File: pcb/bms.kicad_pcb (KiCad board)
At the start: 2 copper layers, 202 x 60 mm, 47 parts, among them J1 C0, J10 Taps 6-8, J11 Taps 0-5, J12 Taps 6-8, J13 Taps 0-5, J2 C1, J3 C2, J4 C3, J5 C4, J6 C5, J7 C6, J8 C7, J9 C8, U1 BQ76942PFBR

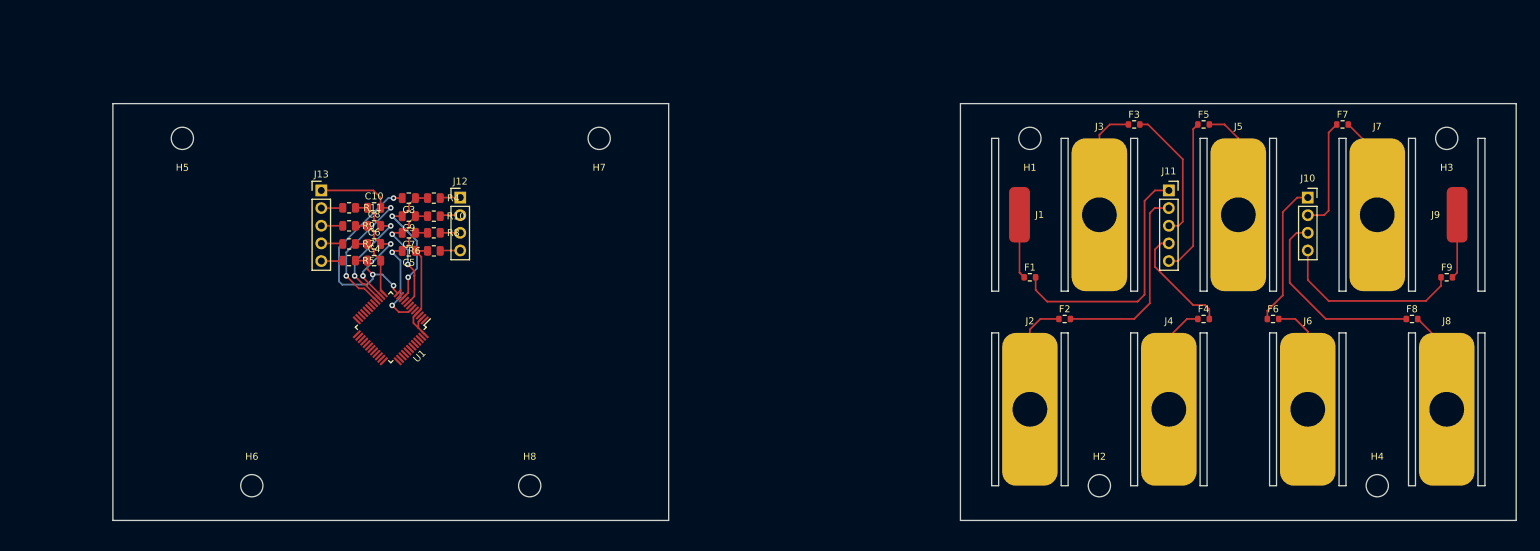
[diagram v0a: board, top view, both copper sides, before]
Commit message: AFE mostly complete
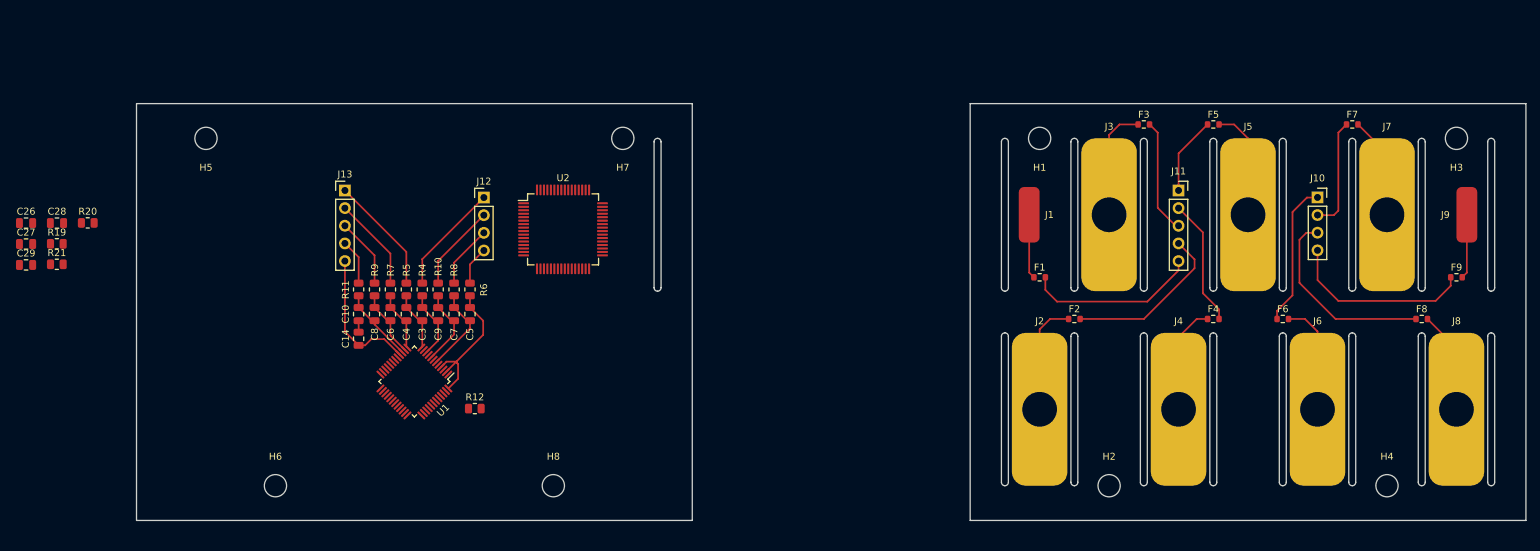
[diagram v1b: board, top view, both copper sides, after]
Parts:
- added C14: 220n, Capacitor_SMD:C_0805_2012Metric, F.Cu at (82.0, 93.8)
- added C26: 22n, Capacitor_SMD:C_0805_2012Metric, F.Cu at (34.1, 77.2)
- added C27: 1u, Capacitor_SMD:C_0805_2012Metric, F.Cu at (34.1, 80.2)
- added C28: 1u, Capacitor_SMD:C_0805_2012Metric, F.Cu at (38.5, 77.2)
- added C29: 1u, Capacitor_SMD:C_0805_2012Metric, F.Cu at (34.1, 83.2)
- added R12: 100, Resistor_SMD:R_0805_2012Metric, F.Cu at (98.7, 103.9)
- added R19: 10k, Resistor_SMD:R_0805_2012Metric, F.Cu at (38.5, 80.2)
- added R20: 150, Resistor_SMD:R_0805_2012Metric, F.Cu at (43.0, 77.2)
- added R21: 150, Resistor_SMD:R_0805_2012Metric, F.Cu at (38.5, 83.1)
- added U2: STM32F405RGTx, Package_QFP:LQFP-64_10x10mm_P0.5mm, F.Cu at (111.4, 78.1)
- moved C3 16.8 mm to (91.1, 90.3), turned to 270 degrees
- moved C10 15.5 mm to (82.0, 90.3), turned to 270 degrees
- moved C9 14.7 mm to (93.4, 90.3), turned to 270 degrees
- moved C7 13.4 mm to (95.7, 90.3), turned to 270 degrees
- moved R4 13.3 mm to (91.1, 86.8), turned to 270 degrees
- moved C8 12.7 mm to (84.3, 90.3), turned to 270 degrees
- moved C5 12.7 mm to (98.0, 90.3), turned to 270 degrees
- moved R11 11.8 mm to (82.0, 86.8), turned to 270 degrees
- moved R10 10.6 mm to (93.4, 86.8), turned to 270 degrees
- moved C6 10.4 mm to (86.6, 90.3), turned to 270 degrees
- moved R9 9.86 mm to (84.3, 86.8), turned to 270 degrees
- moved R5 9.23 mm to (88.8, 86.8), turned to 270 degrees
- moved C4 8.99 mm to (88.8, 90.3), turned to 270 degrees
- moved R7 8.85 mm to (86.6, 86.8), turned to 270 degrees
- moved R8 8.65 mm to (95.7, 86.8), turned to 270 degrees
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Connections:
- net Net-(F3-Pad2) renamed /Cell Interconnect/C2
- net Net-(F6-Pad1) renamed /Cell Interconnect/C5
- net Net-(F7-Pad1) renamed /Cell Interconnect/C6
- net Net-(F8-Pad1) renamed /Cell Interconnect/C7
- net Net-(F9-Pad1) renamed /Cell Interconnect/C8
- net Net-(J12-Pad1) renamed /Cell Measurement/C5
- net Net-(J12-Pad2) renamed /Cell Measurement/C6
- net Net-(J12-Pad3) renamed /Cell Measurement/C7
- net Net-(J12-Pad4) renamed /Cell Measurement/C8
- net Net-(J13-Pad3) renamed /Cell Measurement/C2
- net Net-(U1-Pad21) renamed /Cell Measurement/TS1
- net Net-(U1-Pad23) renamed /Cell Measurement/TS3
- C10 pad 2: Net-(C10-Pad2) -> GND
- F1 pad 2: Net-(F1-Pad2) -> /Cell Interconnect/C0
- F2 pad 2: Net-(F2-Pad2) -> /Cell Interconnect/C1
- F4 pad 2: Net-(F4-Pad2) -> /Cell Interconnect/C3
- F5 pad 1: Net-(F5-Pad1) -> /Cell Interconnect/C4
- J11 pad 1: Net-(F1-Pad2) -> /Cell Interconnect/C4
- J11 pad 2: Net-(F2-Pad2) -> /Cell Interconnect/C3
- J11 pad 4: Net-(F4-Pad2) -> /Cell Interconnect/C1
- J11 pad 5: Net-(F5-Pad1) -> /Cell Interconnect/C0
- J13 pad 1: Net-(C10-Pad2) -> /Cell Measurement/C4
- J13 pad 2: Net-(J13-Pad2) -> /Cell Measurement/C3
- J13 pad 4: Net-(J13-Pad4) -> /Cell Measurement/C1
- J13 pad 5: Net-(J13-Pad5) -> /Cell Measurement/C0
- R11 pad 1: Net-(J13-Pad2) -> /Cell Measurement/C1
- R5 pad 1: Net-(J13-Pad5) -> /Cell Measurement/C4
- R7 pad 1: Net-(J13-Pad4) -> /Cell Measurement/C3
- U1 pad 16: Net-(C10-Pad2) -> /Cell Measurement/C0
- U1 pad 34: Net-(U1-Pad34) -> +3V3
- U1 pad 35: Net-(U1-Pad35) -> +3V3
- U1 pad 47: Net-(U1-Pad47) -> /Cell Measurement/BAT
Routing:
- net Net-(F1-Pad2): track 36.2 -> 0.00 mm
- net Net-(C10-Pad2): track 30.2 -> 0.00 mm, vias 2 -> 0
- net Net-(F2-Pad2): track 28.4 -> 0.00 mm
- net /Cell Interconnect/C0: track 0.00 -> 24.9 mm
- net /Cell Interconnect/C1: track 0.00 -> 24.0 mm
- net Net-(C3-Pad2): track 32.0 -> 8.68 mm, vias 3 -> 0
- net Net-(F5-Pad1): track 22.2 -> 0.00 mm
- net /Cell Measurement/C0: track 0.00 -> 21.0 mm
- net /Cell Interconnect/C3: track 0.00 -> 18.4 mm
- net /Cell Measurement/C4: track 0.00 -> 17.0 mm
- net Net-(F4-Pad2): track 16.6 -> 0.00 mm
- net /Cell Measurement/C3: track 0.00 -> 13.5 mm
- net /Cell Measurement/C5: track 2.92 -> 16.0 mm
- net /Cell Interconnect/C4: track 0.00 -> 11.2 mm
- net Net-(C3-Pad1): track 20.7 -> 10.0 mm, vias 2 -> 0
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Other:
- board size 202 x 60 mm -> 200 x 60 mm

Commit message: microcontroller added
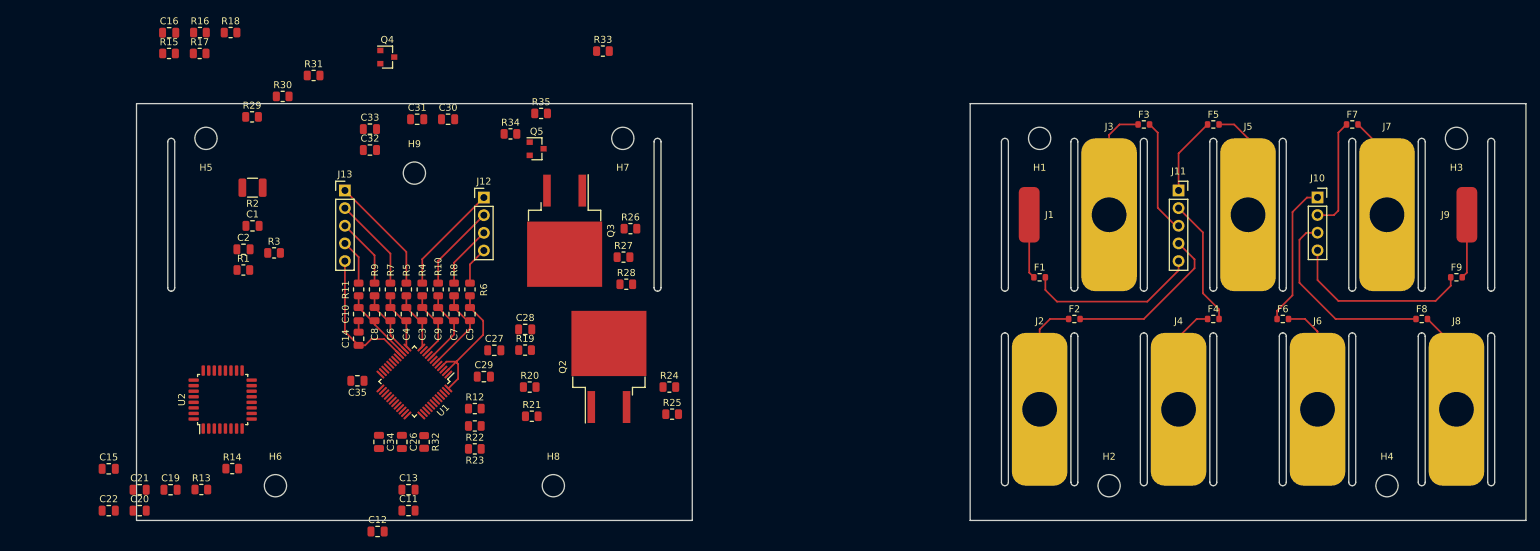
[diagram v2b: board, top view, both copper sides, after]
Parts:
- added C1: 100p, Capacitor_SMD:C_0805_2012Metric, F.Cu at (66.7, 77.6)
- added C11: 1u, Capacitor_SMD:C_0805_2012Metric, F.Cu at (89.2, 118.6)
- added C12: 100p, Capacitor_SMD:C_0805_2012Metric, F.Cu at (84.7, 121.6)
- added C13: 0.47u, Capacitor_SMD:C_0805_2012Metric, F.Cu at (89.2, 115.6)
- added C15: 4.7u, Capacitor_SMD:C_0805_2012Metric, F.Cu at (46.0, 112.6)
- added C16: 100n, Capacitor_SMD:C_0805_2012Metric, F.Cu at (54.7, 49.8)
- added C19: 0.1u, Capacitor_SMD:C_0805_2012Metric, F.Cu at (54.9, 115.6)
- added C2: 0.1u, Capacitor_SMD:C_0805_2012Metric, F.Cu at (65.4, 81.0)
- added C20: 0.1u, Capacitor_SMD:C_0805_2012Metric, F.Cu at (50.5, 118.6)
- added C21: 1u, Capacitor_SMD:C_0805_2012Metric, F.Cu at (50.5, 115.6)
- added C22: 10n, Capacitor_SMD:C_0805_2012Metric, F.Cu at (46.0, 118.6)
- added C30: 0.1u, Capacitor_SMD:C_0805_2012Metric, F.Cu at (94.8, 62.2)
- added C31: 0.1u, Capacitor_SMD:C_0805_2012Metric, F.Cu at (90.4, 62.2)
- added C32: 0.1u, Capacitor_SMD:C_0805_2012Metric, F.Cu at (83.6, 66.7)
- added C33: 0.1u, Capacitor_SMD:C_0805_2012Metric, F.Cu at (83.6, 63.7)
- added C34: 0.1u, Capacitor_SMD:C_0805_2012Metric, F.Cu at (84.9, 108.7)
- added C35: 2.2u, Capacitor_SMD:C_0805_2012Metric, F.Cu at (81.8, 99.9)
- added H9: MountingHole, MountingHole:MountingHole_3.2mm_M3, F.Cu at (90.0, 70.0)
- added Q2: CSD19506KTT, Package_TO_SOT_SMD:TO-263-2, F.Cu at (118.0, 97.9)
- added Q3: CSD19506KTT, Package_TO_SOT_SMD:TO-263-2, F.Cu at (111.6, 78.3)
- added Q4: ZXMP10A13FTA, Package_TO_SOT_SMD:SOT-23, F.Cu at (86.1, 53.3)
- added Q5: ZXMP10A13FTA, Package_TO_SOT_SMD:SOT-23, F.Cu at (107.6, 66.5)
- added R1: 100, Resistor_SMD:R_0805_2012Metric, F.Cu at (65.4, 84.0)
- added R13: 22, Resistor_SMD:R_0805_2012Metric, F.Cu at (59.3, 115.5)
- added R14: 22, Resistor_SMD:R_0805_2012Metric, F.Cu at (63.8, 112.5)
- added R15: 10k, Resistor_SMD:R_0805_2012Metric, F.Cu at (54.7, 52.8)
- added R16: 10k, Resistor_SMD:R_0805_2012Metric, F.Cu at (59.1, 49.8)
- added R17: 10k, Resistor_SMD:R_0805_2012Metric, F.Cu at (59.1, 52.8)
- added R18: 10k, Resistor_SMD:R_0805_2012Metric, F.Cu at (63.5, 49.8)
- added R2: 2m, Resistor_SMD:R_1210_3225Metric, F.Cu at (66.7, 72.1)
- added R22: 10k, Resistor_SMD:R_0805_2012Metric, F.Cu at (98.7, 106.4)
- added R23: 10k, Resistor_SMD:R_0805_2012Metric, F.Cu at (98.7, 109.7)
- added R24: 10k, Resistor_SMD:R_0805_2012Metric, F.Cu at (126.7, 100.8)
- added R25: 5.1k, Resistor_SMD:R_0805_2012Metric, F.Cu at (127.1, 104.7)
- added R26: 10k, Resistor_SMD:R_0805_2012Metric, F.Cu at (121.1, 78.0)
- added R27: 10k, Resistor_SMD:R_0805_2012Metric, F.Cu at (120.1, 82.1)
- added R28: 1k, Resistor_SMD:R_0805_2012Metric, F.Cu at (120.5, 86.0)
- added R29: 3.9k, Resistor_SMD:R_0805_2012Metric, F.Cu at (66.6, 61.9)
- added R3: 100, Resistor_SMD:R_0805_2012Metric, F.Cu at (69.8, 81.5)
- added R30: 1M, Resistor_SMD:R_0805_2012Metric, F.Cu at (71.0, 59.0)
- added R31: 5.1k, Resistor_SMD:R_0805_2012Metric, F.Cu at (75.5, 56.0)
- added R32: 10M, Resistor_SMD:R_0805_2012Metric, F.Cu at (91.4, 108.7)
- added R33: 5.1k, Resistor_SMD:R_0805_2012Metric, F.Cu at (117.1, 52.4)
- added R34: 1M, Resistor_SMD:R_0805_2012Metric, F.Cu at (103.8, 64.4)
- added R35: 3.9k, Resistor_SMD:R_0805_2012Metric, F.Cu at (108.2, 61.4)
- U2: value STM32F405RGTx -> STM32L422KBTx; footprint Package_QFP:LQFP-64_10x10mm_P0.5mm -> Package_QFP:LQFP-32_7x7mm_P0.8mm
- moved R21 71.8 mm to (106.9, 105.0)
- moved C27 69.1 mm to (101.5, 95.5)
- moved C28 69.1 mm to (106.0, 92.5)
- moved R19 69.1 mm to (105.9, 95.5)
- moved R20 67.9 mm to (106.6, 100.8)
- moved C29 67.8 mm to (100.0, 99.3)
- moved C26 62.6 mm to (88.2, 108.7), turned to 270 degrees
- moved U2 54.8 mm to (62.4, 102.6), turned to 90 degrees
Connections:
- net /Cell Measurement/BAT renamed Net-(C11-Pad1)
- R12 pad 2: Net-(D1-Pad1) -> (no net)
- R20 pad 2: Net-(D2-Pad1) -> (no net)
- U1 pad 1: Net-(U1-Pad1) -> (no net)
- U1 pad 11: Net-(U1-Pad11) -> (no net)
- U1 pad 19: Net-(U1-Pad19) -> (no net)
- U1 pad 21: /Cell Measurement/TS1 -> (no net)
- U1 pad 22: Net-(U1-Pad22) -> (no net)
- U1 pad 23: /Cell Measurement/TS3 -> (no net)
- U1 pad 25: Net-(U1-Pad25) -> /Cell Measurement/ALERT
- U1 pad 26: Net-(U1-Pad26) -> /Cell Measurement/SCLK
- U1 pad 27: Net-(U1-Pad27) -> /Cell Measurement/MISO
- U1 pad 28: Net-(U1-Pad28) -> /Cell Measurement/MOSI
- U1 pad 29: Net-(U1-Pad29) -> /Cell Measurement/CFETOFF|CS
- U1 pad 3: Net-(U1-Pad3) -> (no net)
- U1 pad 30: Net-(U1-Pad30) -> /Cell Measurement/DFETOFF
- U1 pad 31: Net-(U1-Pad31) -> /Cell Measurement/DCHG
- U1 pad 32: Net-(U1-Pad32) -> /Cell Measurement/DDSG
- U1 pad 38: Net-(U1-Pad38) -> (no net)
- U1 pad 39: Net-(U1-Pad39) -> /Cell Measurement/PDSG
- U1 pad 40: Net-(U1-Pad40) -> /Cell Measurement/PCHG
- U1 pad 41: Net-(U1-Pad41) -> /Cell Measurement/LD
- U1 pad 42: Net-(U1-Pad42) -> /Cell Measurement/PACK
- U1 pad 43: Net-(U1-Pad43) -> /Cell Measurement/DSG
- U1 pad 44: Net-(U1-Pad44) -> (no net)
- U1 pad 45: Net-(U1-Pad45) -> /Cell Measurement/CHG
- U1 pad 5: Net-(U1-Pad5) -> (no net)
- U1 pad 7: Net-(U1-Pad7) -> (no net)
- U1 pad 9: Net-(U1-Pad9) -> (no net)
- U2 pad 10: Net-(U2-Pad10) -> /Cell Measurement/CFETOFF|CS
- U2 pad 11: Net-(U2-Pad11) -> /Cell Measurement/SCLK
- U2 pad 12: GND -> /Cell Measurement/MISO
- U2 pad 13: +3V3 -> /Cell Measurement/MOSI
- U2 pad 14: Net-(U2-Pad14) -> /Cell Measurement/DDSG
- U2 pad 15: Net-(U2-Pad15) -> /Cell Measurement/DCHG
- U2 pad 16: Net-(U2-Pad16) -> GND
- U2 pad 17: Net-(U2-Pad17) -> +3V3
- U2 pad 18: GND -> (no net)
- U2 pad 19: +3V3 -> (no net)
- U2 pad 2: Net-(U2-Pad2) -> (no net)
- U2 pad 20: Net-(U2-Pad20) -> (no net)
- U2 pad 21: /Microcontroller/SPI1_CLK -> Net-(R13-Pad2)
- U2 pad 22: /Microcontroller/SPI1_MISO -> Net-(R14-Pad2)
- U2 pad 23: /Microcontroller/SPI1_MOSI -> (no net)
- U2 pad 24: Net-(U2-Pad24) -> (no net)
- U2 pad 25: Net-(U2-Pad25) -> (no net)
- U2 pad 26: Net-(U2-Pad26) -> /Cell Measurement/DFETOFF
- U2 pad 27: Net-(U2-Pad27) -> /Cell Measurement/ALERT
- U2 pad 28: /Microcontroller/BOOT2 -> (no net)
- U2 pad 29: Net-(U2-Pad29) -> (no net)
- U2 pad 3: Net-(U2-Pad3) -> (no net)
- U2 pad 30: Net-(U2-Pad30) -> (no net)
- U2 pad 32: +3V3 -> GND
- U2 pad 4: Net-(U2-Pad4) -> /Microcontroller/NRST
- U2 pad 5: Net-(U2-Pad5) -> +3V3
- U2 pad 6: Net-(U2-Pad6) -> (no net)
- U2 pad 7: Net-(R15-Pad1) (its old number) -> (no net)
- U2 pad 8: Net-(U2-Pad8) -> /Microcontroller/USART2_TX
- U2 pad 9: Net-(U2-Pad9) -> /Microcontroller/USART2_RX
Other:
- outline, holes or cut-outs redrawn
